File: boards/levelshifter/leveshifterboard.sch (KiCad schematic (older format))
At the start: 50 parts

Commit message: Swicthed to integrated level shifter
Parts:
- removed Q? (x4): NDS355, ~, symbol NDS355
- removed Q? (x4): BC817, ~, symbol NPN
- removed R? (x4): 680, ~, symbol R
- removed R? (x4): 1k, ~, symbol R
- removed R? (x4): 180, ~, symbol R
- added C?: C, ~, symbol C
- added R? (x4): 1k, ~, symbol R
- added U?: 74HCT125, ~, symbol 74HCT125
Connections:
- wire segments 127 -> 115
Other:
- moved on the sheet: C?, D?, R?, RV?, SW?, U?, U?A, U?B

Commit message: First version of levelshifter board
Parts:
- removed C? (x2): 100nF, ~, symbol C
- removed P?: CONN_6, ~, symbol CONN_6
- removed Q?: MOSFET_P, ~, symbol MOSFET_P
- removed R? (x4): 1k, ~, symbol R
- added C1: 100n, ~, symbol C
- added C7: 100nf, ~, symbol C
- added P2: CONN_7, ~, symbol CONN_7
- added Q1: IRLR110, ~, symbol IRLR110
- added Q2: NDS355, ~, symbol NDS355
- added R11, R12: 1k, ~, symbol R
- added R4: 100k, ~, symbol R
- C2: renamed from C?; value C -> 100nf
- R6: renamed from R?; value 20k -> 1k
- R8: renamed from R?; value 10k -> 1k
- gave numbers to parts that had none: 24
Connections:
- net +24V: now also Q1.2 (D)
- net +3.3V: now also P2.1 (P1), R12.1
- net +5V: now also C7.1
- net 3.3_Clock: now also P2.2 (P2)
- net 3.3_Data_Out: now also P2.3 (P3)
- net 3.3_Enable: now also P2.4 (P4)
- net 3.3_Reset: now also P2.5 (P5)
- net GND: now also C1.2, C7.2, P2.7 (P7), Q2.3 (S); no longer U3.1 (OE1), U3.10 (OE3), U3.13 (OE4), U3.4 (OE2)
- net PowerOn: now also U2.3 (notQ), Q1.1 (G); no longer U2.5 (Q)
- net Shutdown: now also R6.2, U2.7 (PRE); no longer R8.1, U2.6 (CLR)
- net at J1.2, J1.4: now also Q1.3 (S)
- net at R2.2, U1.1: now also R4.1; no longer U1.6 (-)
- net at R7.2: now also D1.1 (A); no longer U2.3 (notQ)
- net BusOff: now reaches R7.1
- net BusOff: now also U2.5 (Q), U3.1 (OE1), U3.10 (OE3), U3.13 (OE4), U3.4 (OE2), R11.1; no longer D1.1 (A)
- new net: C1.1, R4.2, U1.6 (-)
- new net: R8.1, SW1.1, U2.6 (CLR)
- new net: P2.6 (P6), Q2.2 (D), R12.2
- new net: Q2.1 (G), R11.2
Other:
- moved on the sheet: C2, C3, C4, C5, C6, D1, D2, D3, D4, J1, R1, R10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

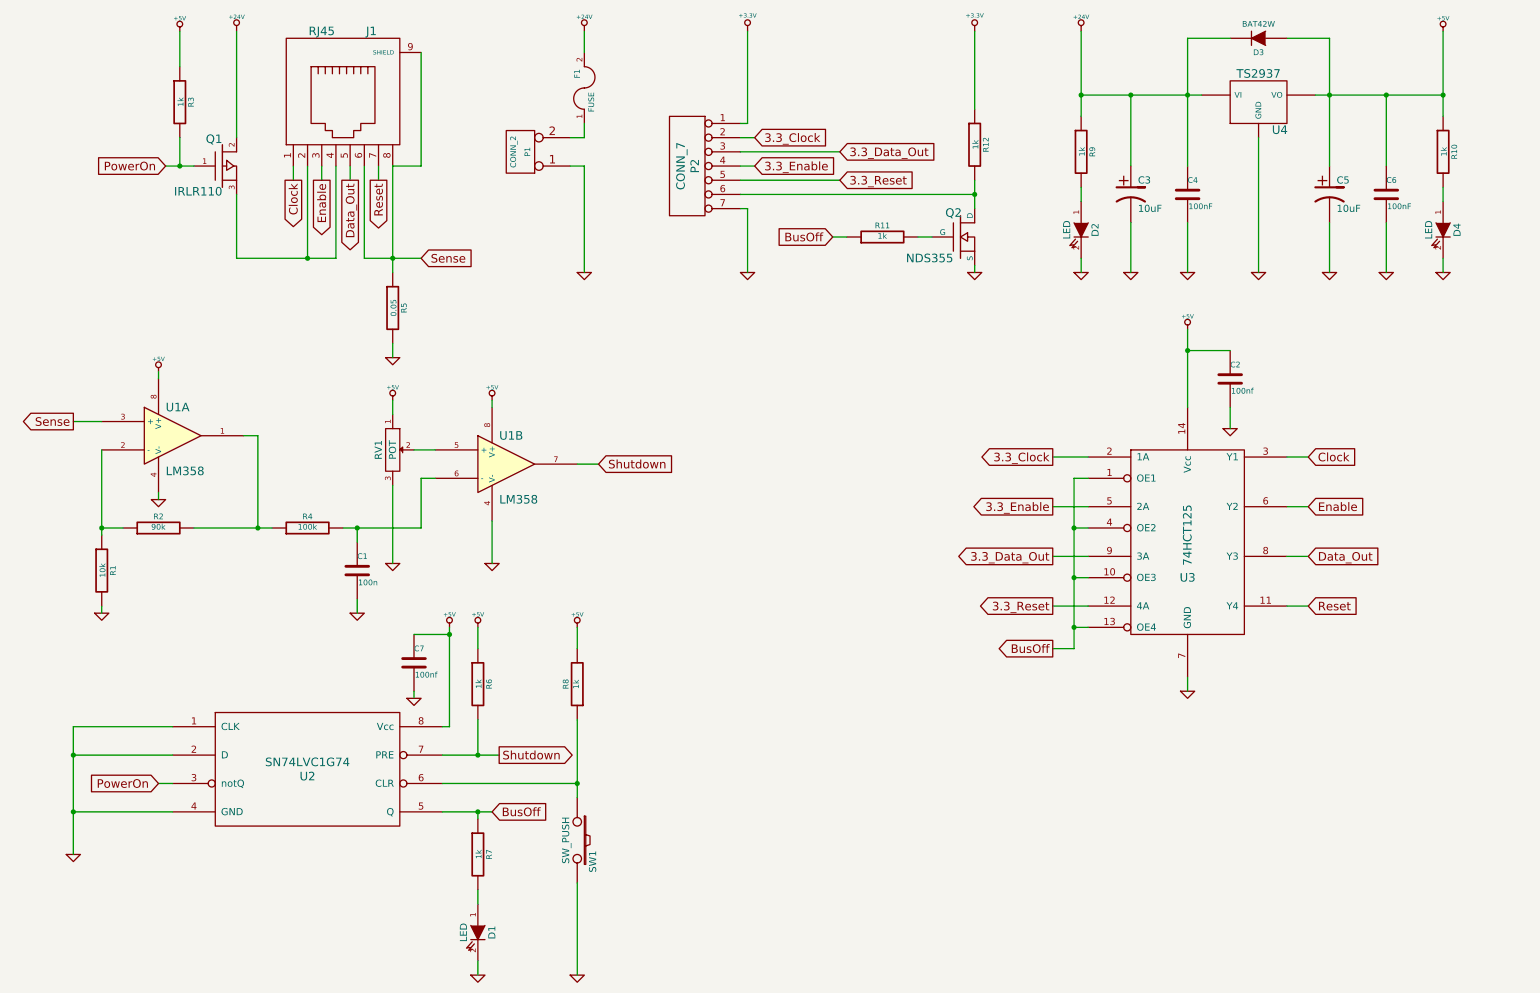
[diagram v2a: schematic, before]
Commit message: Updated levelshifter schematic
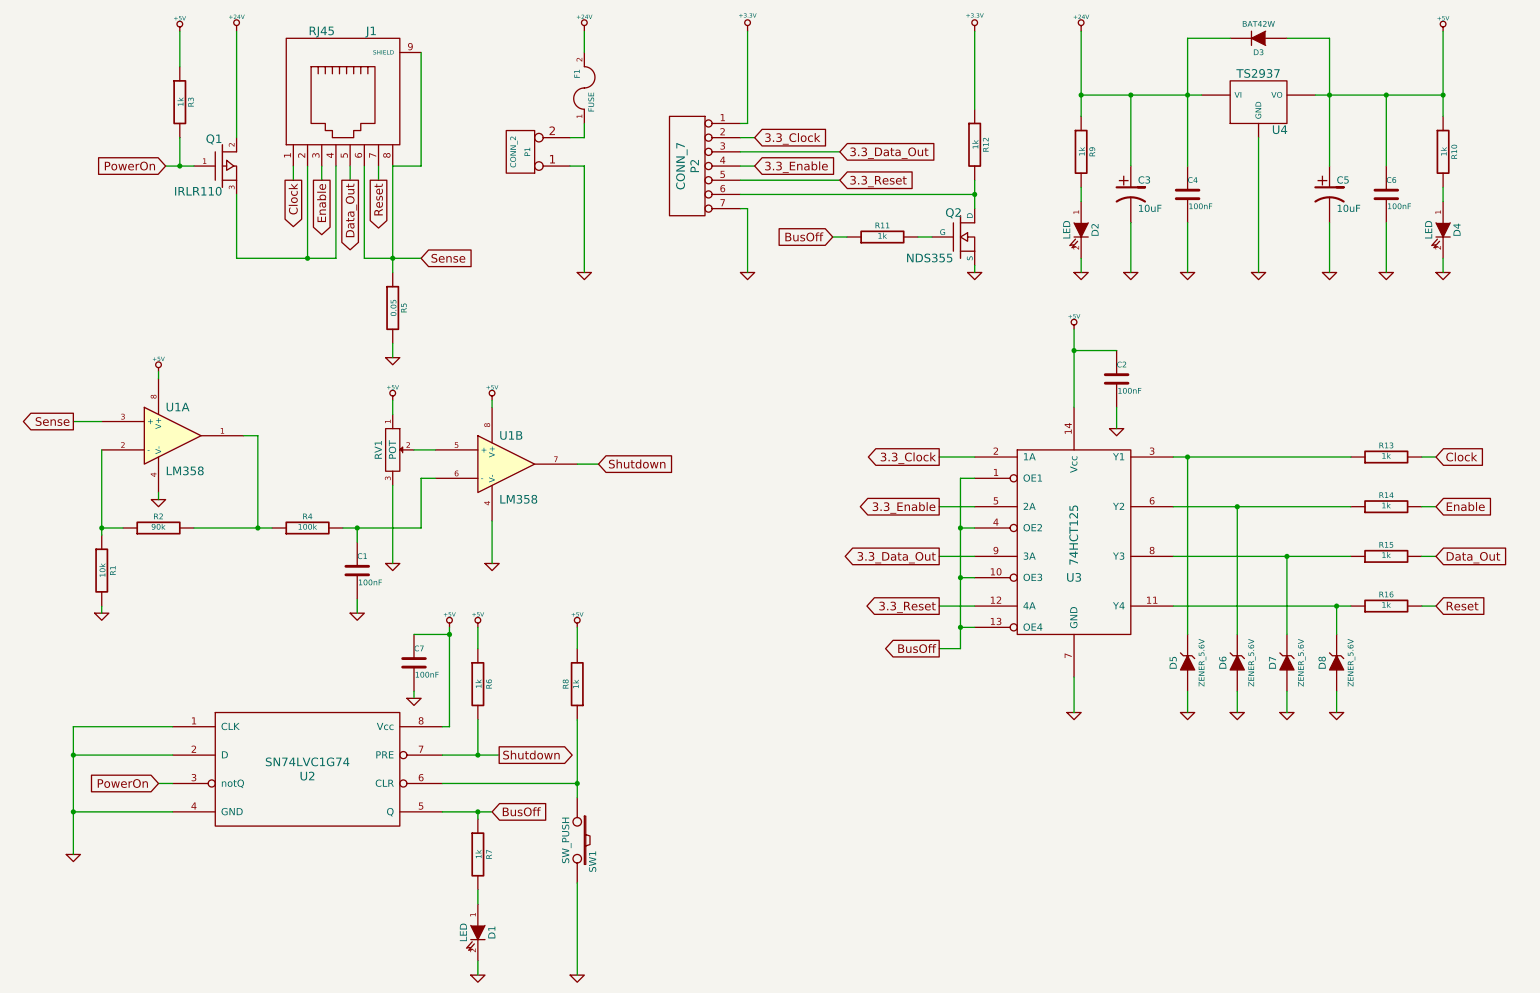
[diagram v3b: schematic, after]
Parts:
- added D5, D6, D7, D8: ZENER_5.6V, ~, symbol ZENER
- added R13, R14, R15, R16: 1k, ~, symbol R
- C1: value 100n -> 100nF
- C2, C7: value 100nf -> 100nF
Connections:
- net Clock: now also R13.2; no longer U3.3 (Y1)
- net Data_Out: now also R15.2; no longer U3.8 (Y3)
- net Enable: now also R14.2; no longer U3.6 (Y2)
- net GND: now also D5.1 (A), D6.1 (A), D7.1 (A), D8.1 (A)
- net Reset: now also R16.2; no longer U3.11 (Y4)
- new net: D8.2 (K), R16.1, U3.11 (Y4)
- new net: D5.2 (K), R13.1, U3.3 (Y1)
- new net: D6.2 (K), R14.1, U3.6 (Y2)
- new net: D7.2 (K), R15.1, U3.8 (Y3)
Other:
- moved on the sheet: C2, U3

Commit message: More work on levelshifter
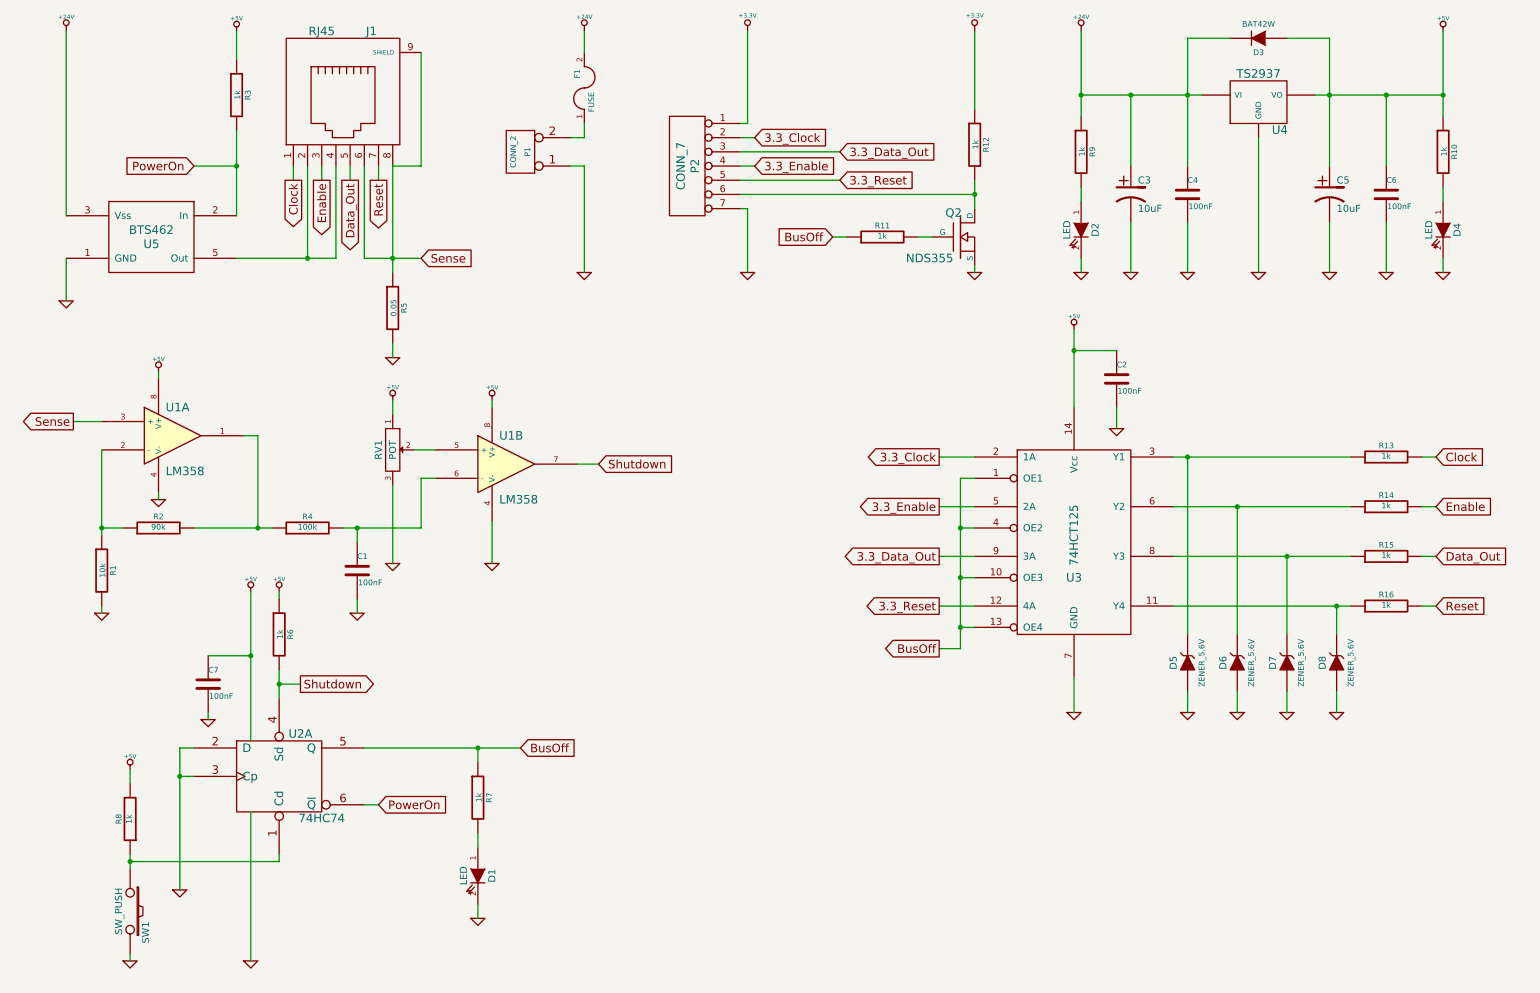
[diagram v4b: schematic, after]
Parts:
- removed Q1: IRLR110, ~, symbol IRLR110
- removed U2: SN74LVC1G74, ~, symbol SN74LVC1G74
- added U2: 74HC74, ~, symbol 74HC74
- added U5: BTS462, ~, symbol BTS462
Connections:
- net +24V: now also U5.3 (Vss)
- net +5V: now also U2.14 (VCC)
- net BusOff: now also U2.5 (Q)
- net GND: now also U2.2 (D), U2.3 (Cp), U2.7 (GND), U5.1 (GND)
- net PowerOn: now also U2.6 (~Q), U5.2 (In)
- net Shutdown: now also U2.4 (Sd)
- net at J1.2, J1.4: now also U5.5 (Out)
- net at R8.1, SW1.1: now also U2.1 (Cd)
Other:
- moved on the sheet: C7, D1, R6, R7, R8, SW1
